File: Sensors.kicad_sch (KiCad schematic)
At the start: 13 parts, among them U13 TPRT9013-33, U2 ICM-42688-P, U3 BMP280, U8 INA230

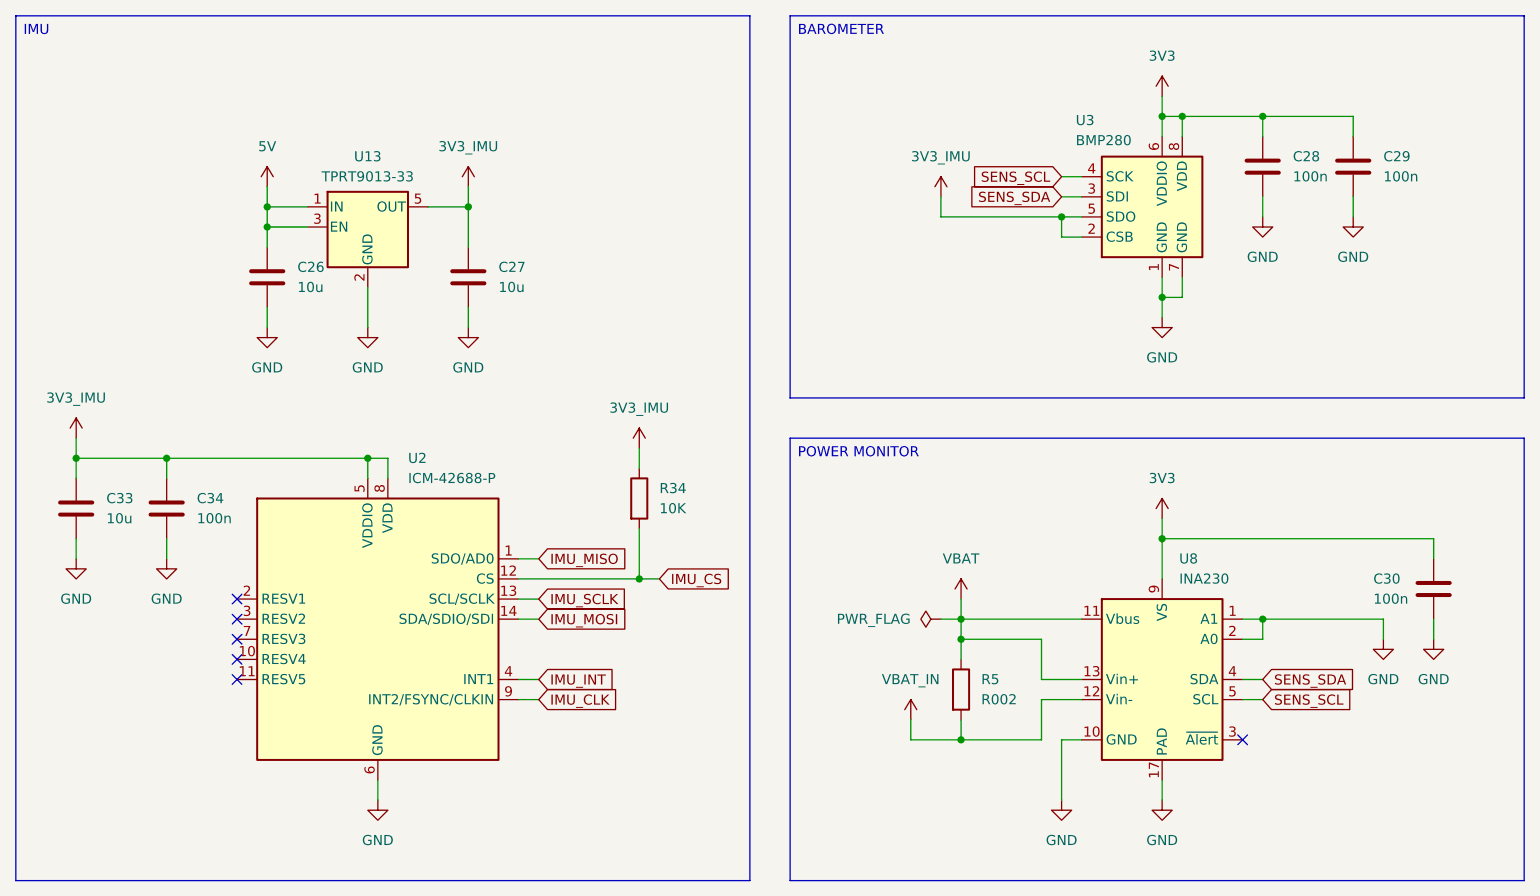
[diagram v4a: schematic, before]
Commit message: Footprints and revision
Added the missing footprints.
Updated a all the schematics.
Completed an initial review of the schematics.

TODO:
Perform a deep review of the schematics before committing to layout.
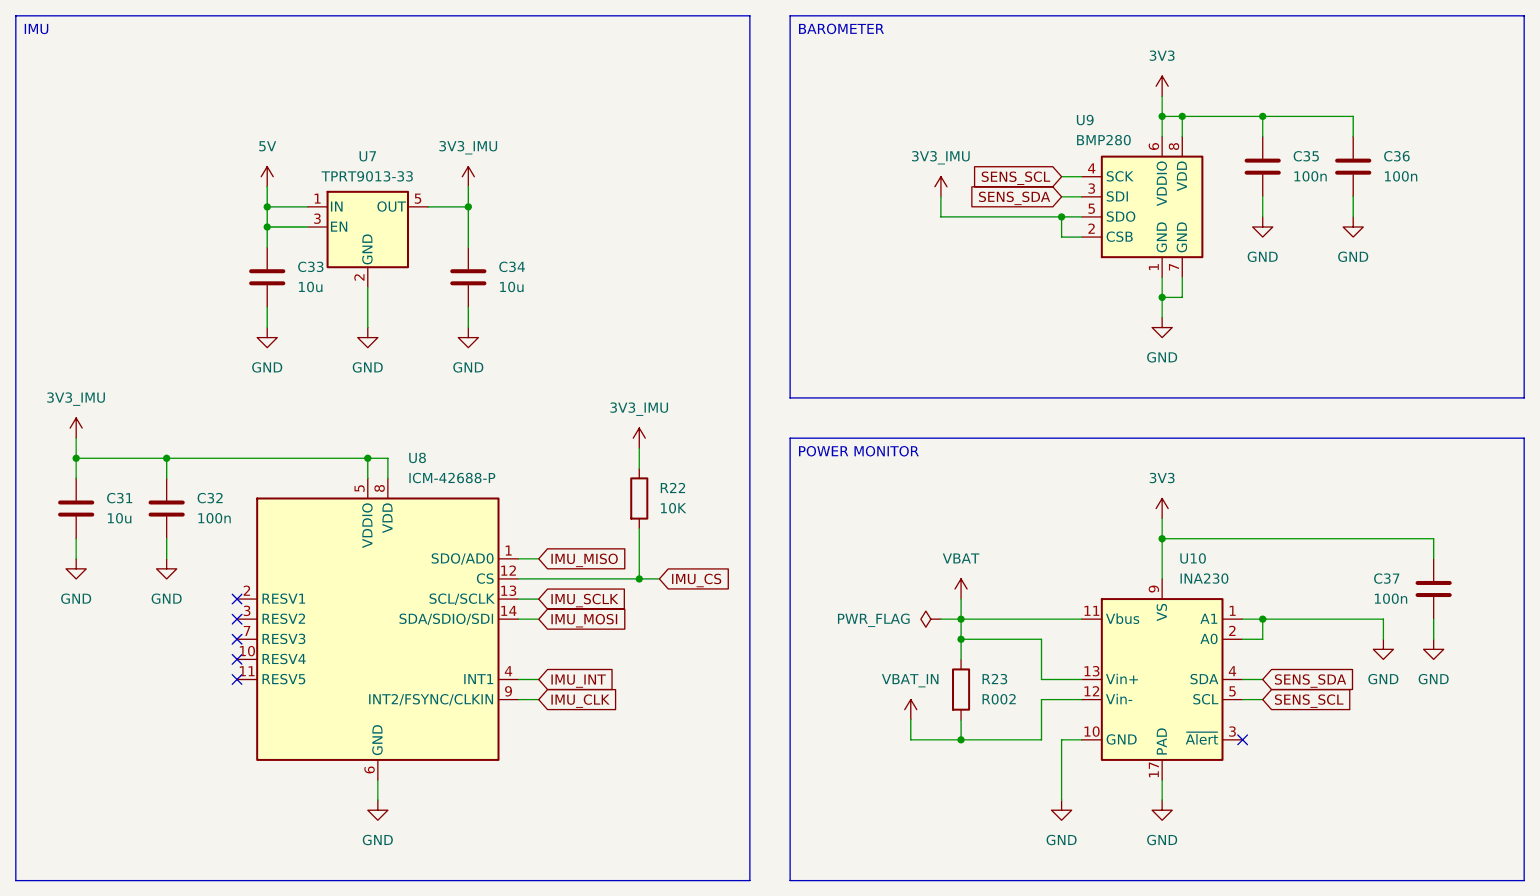
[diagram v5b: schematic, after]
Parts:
- C31: renamed from C33; footprint (none) -> Capacitor_SMD:C_0805_2012Metric
- C32: renamed from C34; footprint (none) -> Capacitor_SMD:C_0603_1608Metric
- C33: renamed from C26; footprint (none) -> Capacitor_SMD:C_0805_2012Metric
- C34: renamed from C27; footprint (none) -> Capacitor_SMD:C_0805_2012Metric
- C35: renamed from C28; footprint (none) -> Capacitor_SMD:C_0201_0603Metric
- C36: renamed from C29; footprint (none) -> Capacitor_SMD:C_0201_0603Metric
- C37: renamed from C30; footprint (none) -> Capacitor_SMD:C_0201_0603Metric
- R22: renamed from R34; footprint (none) -> Resistor_SMD:R_0603_1608Metric
- R23: renamed from R5; footprint (none) -> Resistor_SMD:R_2512_6332Metric
- renumbered U8 to U10, U13 to U7, U2 to U8, U3 to U9

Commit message: Receiver and sensors
Updated the receiver schematic.
Updated the sensors schematic.
Removed the ESP32 C3.
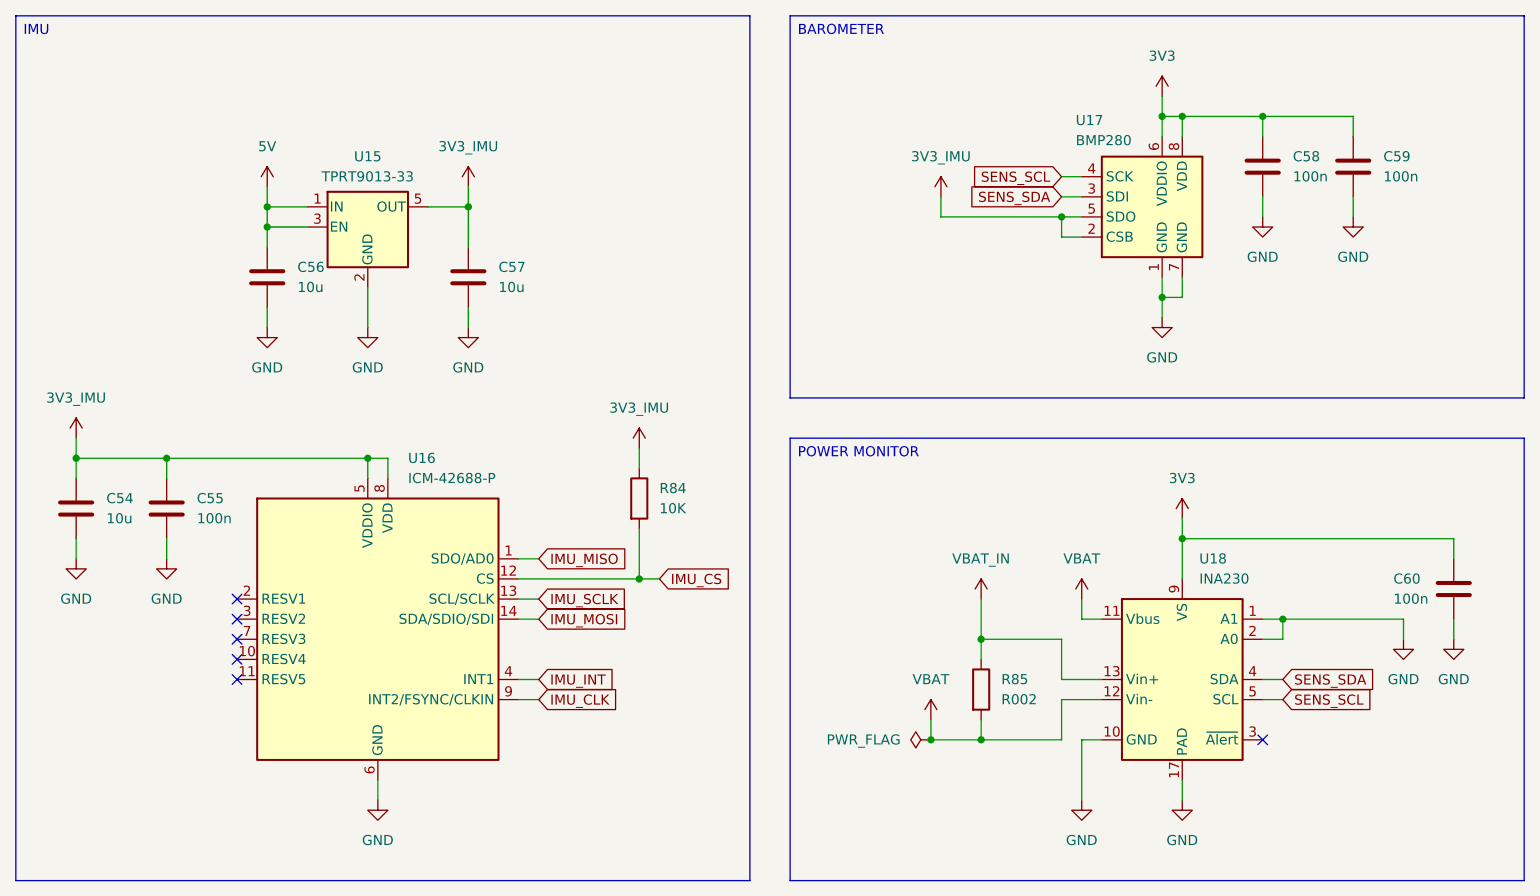
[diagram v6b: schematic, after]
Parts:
- renumbered C31 to C54, C32 to C55, C33 to C56, C34 to C57, C35 to C58, C36 to C59, C37 to C60, R22 to R84, R23 to R85, U7 to U15, U8 to U16, U9 to U17, U10 to U18
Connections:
- net VBAT: now also R85.2, U18.12 (Vin-); no longer R85.1, U18.13 (Vin+)
- net VBAT_IN: now also R85.1, U18.13 (Vin+); no longer R85.2, U18.12 (Vin-)
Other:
- company: Chapuzas S.L. -> DavidMolTor
- moved on the sheet: C60, R85, U18

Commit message: Connectors and tag
Added bulk capacitance for each ESC.
Added SWD connector.
Updated all tags.

TODO:
Add pads for the unconnected GPIO pins.
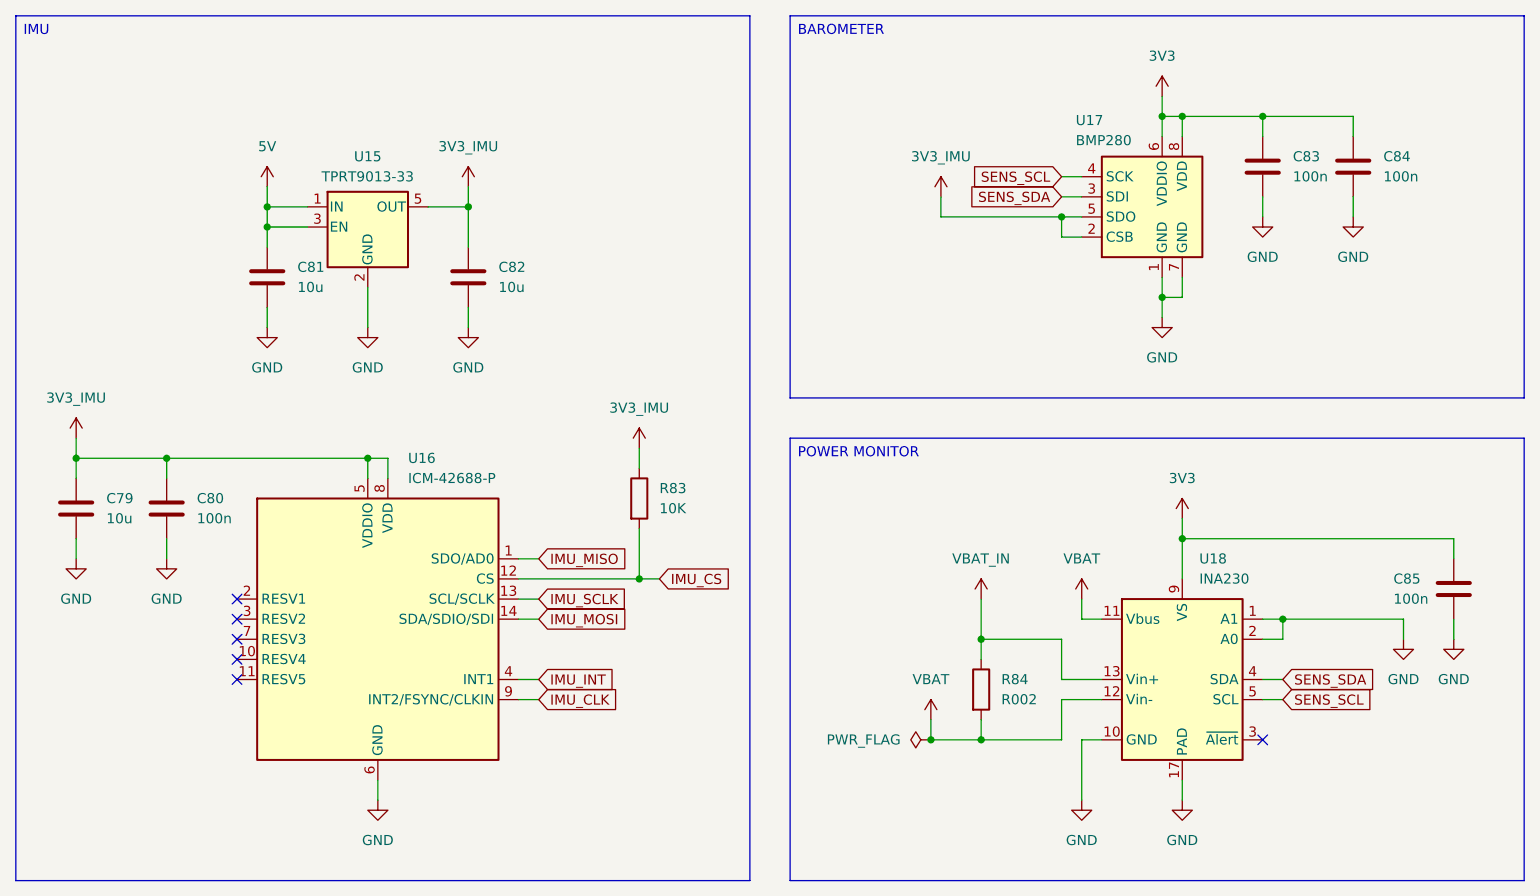
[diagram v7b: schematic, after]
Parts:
- renumbered C54 to C79, C55 to C80, C56 to C81, C57 to C82, C58 to C83, C59 to C84, C60 to C85, R84 to R83, R85 to R84

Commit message: Missing labels and revision
First complete revision of the schematic.
Added missing labels.

TODO:
Continue reviewing the schematic.
Include net coloring.
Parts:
- U18: footprint Custom_Parts:VQFN-16-1EP_3x3mm_P0.5mm_EP1.6x1.6mm_ThermalVias -> Package_DFN_QFN:VQFN-16-1EP_3x3mm_P0.5mm_EP1.6x1.6mm_ThermalVias
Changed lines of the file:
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@@
 			)
 		)
-		(property "Footprint" "Custom_Parts:VQFN-16-1EP_3x3mm_P0.5mm_EP1.6x1.6mm_ThermalVias"
+		(property "Footprint" "Package_DFN_QFN:VQFN-16-1EP_3x3mm_P0.5mm_EP1.6x1.6mm_ThermalVias"
 			(at 220.98 134.62 0)
 			(effects
@@
 		(pin "3"
 		)
+		(pin "8"
+		)
+		(pin "15"
+		)
+		(pin "14"
+		)
+		(pin "7"
+		)
+		(pin "16"
+		)
+		(pin "6"
+		)
 		(instances
